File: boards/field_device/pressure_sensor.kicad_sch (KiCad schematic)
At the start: 4 parts, among them U3 SPA06-003

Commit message: fun
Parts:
- renumbered C6 to C8, C7 to C9, R6 to R9
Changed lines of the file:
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@@
 		(dnp no)
 		(fields_autoplaced yes)
-		(property "Reference" "#PWR012"
+		(property "Reference" "#PWR017"
 			(at 63.5 30.48 0)
 			(hide yes)
@@
 			(project "field_device"
 				(path "/99623870-118f-49fe-bbf0-fb0b890db442/ae167bff-0cee-4447-ad8b-23808a2f268b"
-					(reference "#PWR012")
+					(reference "#PWR017")
 					(unit 1)
 				)
@@
 		(dnp no)
 		(fields_autoplaced yes)
-		(property "Reference" "#PWR010"
+		(property "Reference" "#PWR015"
 			(at 30.48 26.67 0)
 			(hide yes)
@@
 			(project "field_device"
 				(path "/99623870-118f-49fe-bbf0-fb0b890db442/ae167bff-0cee-4447-ad8b-23808a2f268b"
-					(reference "#PWR010")
+					(reference "#PWR015")
 					(unit 1)
 				)
@@
 		(dnp no)
 		(fields_autoplaced yes)
-		(property "Reference" "C6"
+		(property "Reference" "C8"
 			(at 34.29 25.3999 0)
 			(show_name no)
@@
 			(project "field_device"
 				(path "/99623870-118f-49fe-bbf0-fb0b890db442/ae167bff-0cee-4447-ad8b-23808a2f268b"
-					(reference "C6")
+					(reference "C8")
 					(unit 1)
 				)
@@
 		(dnp no)
 		(fields_autoplaced yes)
-		(property "Reference" "#PWR013"
+		(property "Reference" "#PWR018"
 			(at 81.28 24.13 0)
 			(hide yes)
@@
 			(project "field_device"
 				(path "/99623870-118f-49fe-bbf0-fb0b890db442/ae167bff-0cee-4447-ad8b-23808a2f268b"
-					(reference "#PWR013")
+					(reference "#PWR018")
 					(unit 1)
 				)
@@
 		(dnp no)
 		(fields_autoplaced yes)
-		(property "Reference" "#PWR014"
+		(property "Reference" "#PWR019"
 			(at 116.84 26.67 0)
 			(hide yes)
@@
 			(project "field_device"
 				(path "/99623870-118f-49fe-bbf0-fb0b890db442/ae167bff-0cee-4447-ad8b-23808a2f268b"
-					(reference "#PWR014")
+					(reference "#PWR019")
 					(unit 1)
 				)
@@
 		(dnp no)
 		(fields_autoplaced yes)
-		(property "Reference" "R6"
+		(property "Reference" "R9"
 			(at 71.12 20.32 90)
 			(show_name no)
@@
 			(project "field_device"
 				(path "/99623870-118f-49fe-bbf0-fb0b890db442/ae167bff-0cee-4447-ad8b-23808a2f268b"
-					(reference "R6")
+					(reference "R9")
 					(unit 1)
 				)
@@
 		(dnp no)
 		(fields_autoplaced yes)
-		(property "Reference" "C7"
+		(property "Reference" "C9"
 			(at 46.99 25.3999 0)
 			(show_name no)
@@
 			(project "field_device"
 				(path "/99623870-118f-49fe-bbf0-fb0b890db442/ae167bff-0cee-4447-ad8b-23808a2f268b"
-					(reference "C7")
+					(reference "C9")
 					(unit 1)
 				)
@@
 		(dnp no)
 		(fields_autoplaced yes)
-		(property "Reference" "#PWR011"
+		(property "Reference" "#PWR016"
 			(at 30.48 36.83 0)
 			(hide yes)
@@
 			(project "field_device"
 				(path "/99623870-118f-49fe-bbf0-fb0b890db442/ae167bff-0cee-4447-ad8b-23808a2f268b"
-					(reference "#PWR011")
-					(unit 1)
-				)
+					(reference "#PWR016")
+					(unit 1)
+				)

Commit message: reorganized mcu
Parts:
- C8, C9: value 100nF -> 100n
- R9: value 10kΩ? -> 10k?
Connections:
- no-connect marks 0 -> 1
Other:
- moved on the sheet: C8, C9
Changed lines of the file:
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@@
 	(paper "A4")
 	(junction
-		(at 30.48 22.86)
+		(at 125.73 24.13)
 		(diameter 0)
 		(color 0 0 0 0)
 	)
 	(junction
-		(at 43.18 22.86)
+		(at 120.65 24.13)
 		(diameter 0)
 		(color 0 0 0 0)
 	)
 	(junction
-		(at 30.48 30.48)
+		(at 138.43 24.13)
 		(diameter 0)
 		(color 0 0 0 0)
 	)
+	(junction
+		(at 138.43 31.75)
+		(diameter 0)
+		(color 0 0 0 0)
+	)
+	(no_connect
+		(at 110.49 31.75)
+	)
 	(wire
 		(pts
@@
 	(wire
 		(pts
-			(xy 30.48 22.86) (xy 43.18 22.86)
+			(xy 125.73 24.13) (xy 138.43 24.13)
+		)
+		(stroke
+			(width 0)
+			(type default)
+		)
+	)
+	(wire
+		(pts
+			(xy 120.65 24.13) (xy 120.65 29.21)
 		)
 		(stroke
@@
 	(wire
 		(pts
-			(xy 43.18 22.86) (xy 45.72 22.86)
-		)
-		(stroke
-			(width 0)
-			(type default)
-		)
-	)
-	(wire
-		(pts
-			(xy 30.48 30.48) (xy 43.18 30.48)
-		)
-		(stroke
-			(width 0)
-			(type default)
-		)
-	)
-	(label "clean_pwr"
-		(at 110.49 24.13 0)
-		(effects
-			(font
-				(size 1.27 1.27)
-			)
-			(justify left bottom)
-		)
-	)
-	(label "clean_pwr"
-		(at 45.72 22.86 0)
-		(effects
-			(font
-				(size 1.27 1.27)
-			)
-			(justify left bottom)
-		)
-	)
-	(label "clean_pwr"
-		(at 110.49 29.21 0)
-		(effects
-			(font
-				(size 1.27 1.27)
-			)
-			(justify left bottom)
+			(xy 110.49 24.13) (xy 120.65 24.13)
+		)
+		(stroke
+			(width 0)
+			(type default)
+		)
+	)
+	(wire
+		(pts
+			(xy 125.73 31.75) (xy 138.43 31.75)
+		)
+		(stroke
+			(width 0)
+			(type default)
+		)
+	)
+	(wire
+		(pts
+			(xy 120.65 24.13) (xy 125.73 24.13)
+		)
+		(stroke
+			(width 0)
+			(type default)
+		)
+	)
+	(wire
+		(pts
+			(xy 120.65 29.21) (xy 110.49 29.21)
+		)
+		(stroke
+			(width 0)
+			(type default)
 		)
 	)
@@
 	(symbol
 		(lib_id "power:+3.3V")
-		(at 30.48 22.86 0)
+		(at 138.43 24.13 0)
 		(unit 1)
 		(body_style 1)
@@
 		(fields_autoplaced yes)
 		(property "Reference" "#PWR015"
-			(at 30.48 26.67 0)
+			(at 138.43 27.94 0)
 			(hide yes)
 			(show_name no)
@@
 		)
 		(property "Value" "+3.3V"
-			(at 30.48 17.78 0)
+			(at 138.43 19.05 0)
 			(show_name no)
 			(do_not_autoplace no)
@@
 		)
 		(property "Footprint" ""
-			(at 30.48 22.86 0)
+			(at 138.43 24.13 0)
 			(hide yes)
 			(show_name no)
@@
 		)
 		(property "Datasheet" ""
-			(at 30.48 22.86 0)
+			(at 138.43 24.13 0)
 			(hide yes)
 			(show_name no)
@@
 		)
 		(property "Description" "Power symbol creates a global label with name \"+3.3V\""
-			(at 30.48 22.86 0)
+			(at 138.43 24.13 0)
 			(hide yes)
 			(show_name no)
@@
 	(symbol
 		(lib_id "Device:C")
-		(at 30.48 26.67 0)
+		(at 125.73 27.94 0)
 		(unit 1)
 		(body_style 1)
@@
 		(fields_autoplaced yes)
 		(property "Reference" "C8"
-			(at 34.29 25.3999 0)
+			(at 129.54 26.6699 0)
 			(show_name no)
 			(do_not_autoplace no)
@@
 			)
 		)
-		(property "Value" "100nF"
-			(at 34.29 27.9399 0)
+		(property "Value" "100n"
+			(at 129.54 29.2099 0)
 			(show_name no)
 			(do_not_autoplace no)
@@
 		)
 		(property "Footprint" "Capacitor_SMD:C_0603_1608Metric"
-			(at 31.4452 30.48 0)
+			(at 126.6952 31.75 0)
 			(hide yes)
 			(show_name no)
@@
 		)
 		(property "Datasheet" ""
-			(at 30.48 26.67 0)
+			(at 125.73 27.94 0)
 			(hide yes)
 			(show_name no)
@@
 		)
 		(property "Description" "Unpolarized capacitor"
-			(at 30.48 26.67 0)
+			(at 125.73 27.94 0)
 			(hide yes)
 			(show_name no)
@@
 		)
 		(property "Field5" ""
-			(at 30.48 26.67 0)
+			(at 125.73 27.94 0)
 			(hide yes)
 			(show_name no)
@@
 		)
 		(property "Field6" ""
-			(at 30.48 26.67 0)
+			(at 125.73 27.94 0)
 			(hide yes)
 			(show_name no)
@@
 			)
 		)
-		(property "Value" "10kΩ?"
+		(property "Value" "10k?"
 			(at 71.12 22.86 90)
 			(show_name no)
@@
 	(symbol
 		(lib_id "Device:C")
-		(at 43.18 26.67 0)
+		(at 138.43 27.94 0)
 		(unit 1)
 		(body_style 1)
@@
 		(fields_autoplaced yes)
 		(property "Reference" "C9"
-			(at 46.99 25.3999 0)
+			(at 142.24 26.6699 0)
 			(show_name no)
 			(do_not_autoplace no)
@@
 			)
 		)
-		(property "Value" "100nF"
-			(at 46.99 27.9399 0)
+		(property "Value" "100n"
+			(at 142.24 29.2099 0)
 			(show_name no)
 			(do_not_autoplace no)
@@
 		)
 		(property "Footprint" "Capacitor_SMD:C_0603_1608Metric"
-			(at 44.1452 30.48 0)
+			(at 139.3952 31.75 0)
 			(hide yes)
 			(show_name no)
@@
 		)
 		(property "Datasheet" ""
-			(at 43.18 26.67 0)
+			(at 138.43 27.94 0)
 			(hide yes)
 			(show_name no)
@@
 		)
 		(property "Description" "Unpolarized capacitor"
-			(at 43.18 26.67 0)
+			(at 138.43 27.94 0)
 			(hide yes)
 			(show_name no)
@@
 	(symbol
 		(lib_id "power:GND")
-		(at 30.48 30.48 0)
+		(at 138.43 31.75 0)
 		(unit 1)
 		(body_style 1)
@@
 		(fields_autoplaced yes)
 		(property "Reference" "#PWR016"
-			(at 30.48 36.83 0)
+			(at 138.43 38.1 0)
 			(hide yes)
 			(show_name no)
@@
 		)
 		(property "Value" "GND"
-			(at 30.48 35.56 0)
+			(at 138.43 36.83 0)
 			(show_name no)
 			(do_not_autoplace no)
@@
 		)
 		(property "Footprint" ""
-			(at 30.48 30.48 0)
+			(at 138.43 31.75 0)
 			(hide yes)
 			(show_name no)
@@
 		)
 		(property "Datasheet" ""
-			(at 30.48 30.48 0)
+			(at 138.43 31.75 0)
 			(hide yes)
 			(show_name no)
@@
 		)
 		(property "Description" "Power symbol creates a global label with name \"GND\" , ground"
-			(at 30.48 30.48 0)
-			(hide yes)
-			(show_name no)
+			(at 138.43 31.75 0)
+			(hide yes)
+			(show_name no)

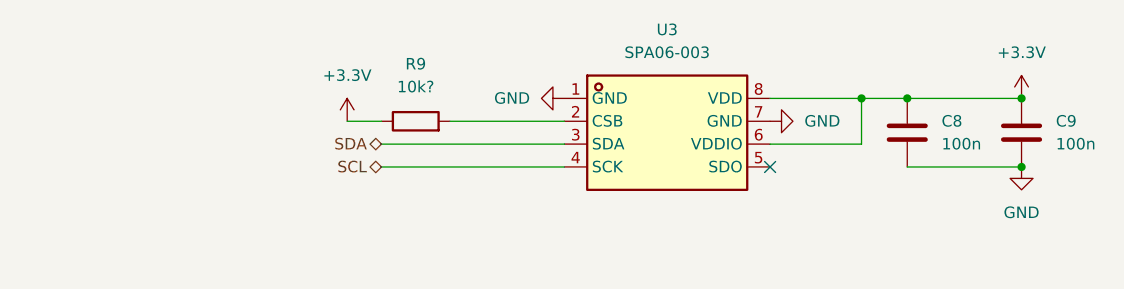
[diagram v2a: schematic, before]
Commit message: added satus leds
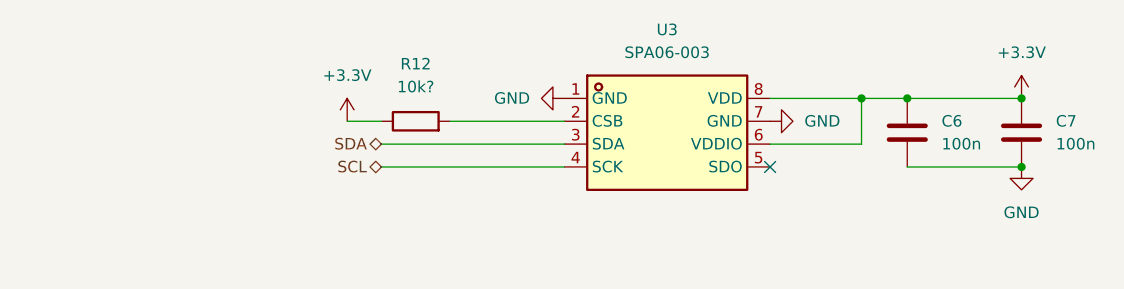
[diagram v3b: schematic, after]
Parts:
- renumbered C8 to C6, C9 to C7, R9 to R12
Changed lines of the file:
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@@
 		(dnp no)
 		(fields_autoplaced yes)
-		(property "Reference" "#PWR017"
+		(property "Reference" "#PWR014"
 			(at 63.5 30.48 0)
 			(hide yes)
@@
 			(project "field_device"
 				(path "/99623870-118f-49fe-bbf0-fb0b890db442/ae167bff-0cee-4447-ad8b-23808a2f268b"
-					(reference "#PWR017")
+					(reference "#PWR014")
 					(unit 1)
 				)
@@
 		(dnp no)
 		(fields_autoplaced yes)
-		(property "Reference" "#PWR015"
+		(property "Reference" "#PWR017"
 			(at 138.43 27.94 0)
 			(hide yes)
@@
 			(project "field_device"
 				(path "/99623870-118f-49fe-bbf0-fb0b890db442/ae167bff-0cee-4447-ad8b-23808a2f268b"
-					(reference "#PWR015")
+					(reference "#PWR017")
 					(unit 1)
 				)
@@
 		(dnp no)
 		(fields_autoplaced yes)
-		(property "Reference" "C8"
+		(property "Reference" "C6"
 			(at 129.54 26.6699 0)
 			(show_name no)
@@
 			(project "field_device"
 				(path "/99623870-118f-49fe-bbf0-fb0b890db442/ae167bff-0cee-4447-ad8b-23808a2f268b"
-					(reference "C8")
+					(reference "C6")
 					(unit 1)
 				)
@@
 		(dnp no)
 		(fields_autoplaced yes)
-		(property "Reference" "#PWR018"
+		(property "Reference" "#PWR015"
 			(at 81.28 24.13 0)
 			(hide yes)
@@
 			(project "field_device"
 				(path "/99623870-118f-49fe-bbf0-fb0b890db442/ae167bff-0cee-4447-ad8b-23808a2f268b"
-					(reference "#PWR018")
+					(reference "#PWR015")
 					(unit 1)
 				)
@@
 		(dnp no)
 		(fields_autoplaced yes)
-		(property "Reference" "#PWR019"
+		(property "Reference" "#PWR016"
 			(at 116.84 26.67 0)
 			(hide yes)
@@
 			(project "field_device"
 				(path "/99623870-118f-49fe-bbf0-fb0b890db442/ae167bff-0cee-4447-ad8b-23808a2f268b"
-					(reference "#PWR019")
+					(reference "#PWR016")
 					(unit 1)
 				)
@@
 		(dnp no)
 		(fields_autoplaced yes)
-		(property "Reference" "R9"
+		(property "Reference" "R12"
 			(at 71.12 20.32 90)
 			(show_name no)
@@
 			(project "field_device"
 				(path "/99623870-118f-49fe-bbf0-fb0b890db442/ae167bff-0cee-4447-ad8b-23808a2f268b"
-					(reference "R9")
+					(reference "R12")
 					(unit 1)
 				)
@@
 		(dnp no)
 		(fields_autoplaced yes)
-		(property "Reference" "C9"
+		(property "Reference" "C7"
 			(at 142.24 26.6699 0)
 			(show_name no)
@@
 			(project "field_device"
 				(path "/99623870-118f-49fe-bbf0-fb0b890db442/ae167bff-0cee-4447-ad8b-23808a2f268b"
-					(reference "C9")
+					(reference "C7")
 					(unit 1)
 				)
@@
 		(dnp no)
 		(fields_autoplaced yes)
-		(property "Reference" "#PWR016"
+		(property "Reference" "#PWR018"
 			(at 138.43 38.1 0)
 			(hide yes)
@@
 			(project "field_device"
 				(path "/99623870-118f-49fe-bbf0-fb0b890db442/ae167bff-0cee-4447-ad8b-23808a2f268b"
-					(reference "#PWR016")
-					(unit 1)
-				)
+					(reference "#PWR018")
+					(unit 1)
+				)

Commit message: i guess made schematic more readable?
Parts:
- C6, C7: footprint Capacitor_SMD:C_0603_1608Metric -> Capacitor_SMD:C_0603_1608Metric_Pad1.08x0.95mm_HandSolder
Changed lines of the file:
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@@
 			)
 		)
-		(property "Footprint" "Capacitor_SMD:C_0603_1608Metric"
+		(property "Footprint" "Capacitor_SMD:C_0603_1608Metric_Pad1.08x0.95mm_HandSolder"
 			(at 126.6952 31.75 0)
 			(hide yes)
@@
 			)
 		)
-		(property "Footprint" "Capacitor_SMD:C_0603_1608Metric"
+		(property "Footprint" "Capacitor_SMD:C_0603_1608Metric_Pad1.08x0.95mm_HandSolder"
 			(at 139.3952 31.75 0)
 			(hide yes)

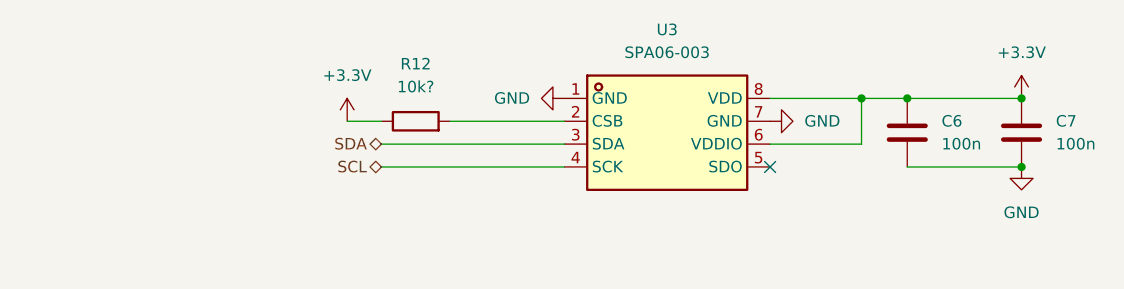
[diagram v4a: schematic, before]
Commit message: changed regulator
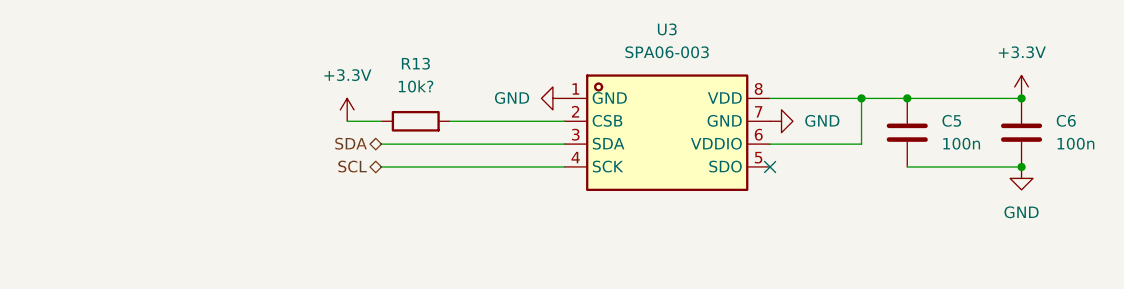
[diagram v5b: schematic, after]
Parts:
- C5: renamed from C6; footprint Capacitor_SMD:C_0603_1608Metric_Pad1.08x0.95mm_HandSolder -> Capacitor_SMD:C_0402_1005Metric_Pad0.74x0.62mm_HandSolder
- C6: renamed from C7; footprint Capacitor_SMD:C_0603_1608Metric_Pad1.08x0.95mm_HandSolder -> Capacitor_SMD:C_0402_1005Metric_Pad0.74x0.62mm_HandSolder
- R13: renamed from R12; footprint Resistor_SMD:R_0603_1608Metric -> Resistor_SMD:R_0402_1005Metric_Pad0.72x0.64mm_HandSolder
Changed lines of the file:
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@@
 		(dnp no)
 		(fields_autoplaced yes)
-		(property "Reference" "C6"
+		(property "Reference" "C5"
 			(at 129.54 26.6699 0)
 			(show_name no)
@@
 			)
 		)
-		(property "Footprint" "Capacitor_SMD:C_0603_1608Metric_Pad1.08x0.95mm_HandSolder"
+		(property "Footprint" "Capacitor_SMD:C_0402_1005Metric_Pad0.74x0.62mm_HandSolder"
 			(at 126.6952 31.75 0)
 			(hide yes)
@@
 			(project "field_device"
 				(path "/99623870-118f-49fe-bbf0-fb0b890db442/ae167bff-0cee-4447-ad8b-23808a2f268b"
-					(reference "C6")
+					(reference "C5")
 					(unit 1)
 				)
@@
 		(dnp no)
 		(fields_autoplaced yes)
-		(property "Reference" "R12"
+		(property "Reference" "R13"
 			(at 71.12 20.32 90)
 			(show_name no)
@@
 			)
 		)
-		(property "Footprint" "Resistor_SMD:R_0603_1608Metric"
+		(property "Footprint" "Resistor_SMD:R_0402_1005Metric_Pad0.72x0.64mm_HandSolder"
 			(at 71.12 28.448 90)
 			(hide yes)
@@
 			(project "field_device"
 				(path "/99623870-118f-49fe-bbf0-fb0b890db442/ae167bff-0cee-4447-ad8b-23808a2f268b"
-					(reference "R12")
+					(reference "R13")
 					(unit 1)
 				)
@@
 		(dnp no)
 		(fields_autoplaced yes)
-		(property "Reference" "C7"
+		(property "Reference" "C6"
 			(at 142.24 26.6699 0)
 			(show_name no)
@@
 			)
 		)
-		(property "Footprint" "Capacitor_SMD:C_0603_1608Metric_Pad1.08x0.95mm_HandSolder"
+		(property "Footprint" "Capacitor_SMD:C_0402_1005Metric_Pad0.74x0.62mm_HandSolder"
 			(at 139.3952 31.75 0)
 			(hide yes)
@@
 			(project "field_device"
 				(path "/99623870-118f-49fe-bbf0-fb0b890db442/ae167bff-0cee-4447-ad8b-23808a2f268b"
-					(reference "C7")
-					(unit 1)
-				)
+					(reference "C6")
+					(unit 1)
+				)

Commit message: route more stuff
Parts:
- C5, C6: footprint Capacitor_SMD:C_0402_1005Metric_Pad0.74x0.62mm_HandSolder -> Capacitor_SMD:C_0603_1608Metric
- R13: footprint Resistor_SMD:R_0402_1005Metric_Pad0.72x0.64mm_HandSolder -> Resistor_SMD:R_0603_1608Metric
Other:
- moved on the sheet: C5
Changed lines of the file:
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@@
 	(paper "A4")
 	(junction
-		(at 125.73 24.13)
-		(diameter 0)
-		(color 0 0 0 0)
-	)
-	(junction
-		(at 120.65 24.13)
+		(at 120.65 29.21)
 		(diameter 0)
 		(color 0 0 0 0)
@@
 		(color 0 0 0 0)
 	)
-	(junction
-		(at 138.43 31.75)
-		(diameter 0)
-		(color 0 0 0 0)
-	)
 	(no_connect
 		(at 110.49 31.75)
@@
 	(wire
 		(pts
-			(xy 125.73 24.13) (xy 138.43 24.13)
+			(xy 67.31 29.21) (xy 87.63 29.21)
 		)
 		(stroke
@@
 	(wire
 		(pts
-			(xy 120.65 24.13) (xy 120.65 29.21)
-		)
-		(stroke
-			(width 0)
-			(type default)
-		)
-	)
-	(wire
-		(pts
-			(xy 67.31 29.21) (xy 87.63 29.21)
-		)
-		(stroke
-			(width 0)
-			(type default)
-		)
-	)
-	(wire
-		(pts
-			(xy 110.49 24.13) (xy 120.65 24.13)
-		)
-		(stroke
-			(width 0)
-			(type default)
-		)
-	)
-	(wire
-		(pts
-			(xy 125.73 31.75) (xy 138.43 31.75)
-		)
-		(stroke
-			(width 0)
-			(type default)
-		)
-	)
-	(wire
-		(pts
-			(xy 120.65 24.13) (xy 125.73 24.13)
+			(xy 110.49 24.13) (xy 138.43 24.13)
 		)
 		(stroke
@@
 	(symbol
 		(lib_id "Device:C")
-		(at 125.73 27.94 0)
+		(at 120.65 33.02 0)
 		(unit 1)
 		(body_style 1)
@@
 		(fields_autoplaced yes)
 		(property "Reference" "C5"
-			(at 129.54 26.6699 0)
+			(at 124.46 31.7499 0)
 			(show_name no)
 			(do_not_autoplace no)
@@
 		)
 		(property "Value" "100n"
-			(at 129.54 29.2099 0)
+			(at 124.46 34.2899 0)
 			(show_name no)
 			(do_not_autoplace no)
@@
 			)
 		)
-		(property "Footprint" "Capacitor_SMD:C_0402_1005Metric_Pad0.74x0.62mm_HandSolder"
-			(at 126.6952 31.75 0)
-			(hide yes)
-			(show_name no)
-			(do_not_autoplace no)
-			(effects
-				(font
-					(size 1.27 1.27)
-				)
-			)
-		)
-		(property "Datasheet" ""
-			(at 125.73 27.94 0)
+		(property "Footprint" "Capacitor_SMD:C_0603_1608Metric"
+			(at 121.6152 36.83 0)
+			(hide yes)
+			(show_name no)
+			(do_not_autoplace no)
+			(effects
+				(font
+					(size 1.27 1.27)
+				)
+			)
+		)
+		(property "Datasheet" ""
+			(at 120.65 33.02 0)
 			(hide yes)
 			(show_name no)
@@
 		)
 		(property "Description" "Unpolarized capacitor"
-			(at 125.73 27.94 0)
+			(at 120.65 33.02 0)
 			(hide yes)
 			(show_name no)
@@
 		)
 		(property "Field5" ""
-			(at 125.73 27.94 0)
+			(at 120.65 33.02 0)
 			(hide yes)
 			(show_name no)
@@
 		)
 		(property "Field6" ""
-			(at 125.73 27.94 0)
+			(at 120.65 33.02 0)
 			(hide yes)
 			(show_name no)
@@
 			)
 		)
-		(property "Footprint" "Resistor_SMD:R_0402_1005Metric_Pad0.72x0.64mm_HandSolder"
+		(property "Footprint" "Resistor_SMD:R_0603_1608Metric"
 			(at 71.12 28.448 90)
 			(hide yes)
@@
 			)
 		)
-		(property "Footprint" "Capacitor_SMD:C_0402_1005Metric_Pad0.74x0.62mm_HandSolder"
+		(property "Footprint" "Capacitor_SMD:C_0603_1608Metric"
 			(at 139.3952 31.75 0)
 			(hide yes)
@@
 					(unit 1)
 				)
+			)
+		)
+	)
+	(symbol
+		(lib_id "power:GND")
+		(at 120.65 36.83 0)
+		(unit 1)
+		(body_style 1)
+		(exclude_from_sim no)
+		(in_bom yes)
+		(on_board yes)
+		(in_pos_files yes)
+		(dnp no)
+		(fields_autoplaced yes)
+		(property "Reference" "#PWR031"
+			(at 120.65 43.18 0)
+			(hide yes)
+			(show_name no)
+			(do_not_autoplace no)
+			(effects
+				(font
+					(size 1.27 1.27)
+				)
+			)
+		)
+		(property "Value" "GND"
+			(at 120.65 41.91 0)
+			(show_name no)
+			(do_not_autoplace no)
+			(effects
+				(font
+					(size 1.27 1.27)
+				)
+			)
+		)
+		(property "Footprint" ""
+			(at 120.65 36.83 0)
+			(hide yes)
+			(show_name no)
+			(do_not_autoplace no)
+			(effects
+				(font
+					(size 1.27 1.27)
+				)
+			)
+		)
+		(property "Datasheet" ""
+			(at 120.65 36.83 0)
+			(hide yes)
+			(show_name no)
+			(do_not_autoplace no)
+			(effects
+				(font
+					(size 1.27 1.27)
+				)
+			)
+		)
+		(property "Description" "Power symbol creates a global label with name \"GND\" , ground"
+			(at 120.65 36.83 0)
+			(hide yes)
+			(show_name no)
+			(do_not_autoplace no)
+			(effects
+				(font
+					(size 1.27 1.27)
+				)
+			)
+		)
+		(pin "1"
+		)
+		(instances
+			(project "field_device"
+				(path "/99623870-118f-49fe-bbf0-fb0b890db442/ae167bff-0cee-4447-ad8b-23808a2f268b"
+					(reference "#PWR031")
+					(unit 1)
+				)
+			)
+		)
+	)
+	(symbol
+		(lib_id "power:+3.3V")
+		(at 120.65 29.21 0)
+		(unit 1)
+		(body_style 1)
+		(exclude_from_sim no)
+		(in_bom yes)
+		(on_board yes)
+		(in_pos_files yes)
+		(dnp no)
+		(property "Reference" "#PWR032"
+			(at 120.65 33.02 0)
+			(hide yes)
+			(show_name no)
+			(do_not_autoplace no)
+			(effects
+				(font
+					(size 1.27 1.27)
+				)
+			)
+		)
+		(property "Value" "+3.3V"
+			(at 120.65 25.4 0)
+			(show_name no)
+			(do_not_autoplace no)
+			(effects
+				(font
+					(size 1.27 1.27)
+				)
+			)
+		)
+		(property "Footprint" ""
+			(at 120.65 29.21 0)
+			(hide yes)
+			(show_name no)
+			(do_not_autoplace no)
+			(effects
+				(font
+					(size 1.27 1.27)
+				)
+			)
+		)
+		(property "Datasheet" ""
+			(at 120.65 29.21 0)
+			(hide yes)
+			(show_name no)
+			(do_not_autoplace no)
+			(effects
+				(font
+					(size 1.27 1.27)
+				)
+			)
+		)
+		(property "Description" "Power symbol creates a global label with name \"+3.3V\""
+			(at 120.65 29.21 0)
+			(hide yes)
+			(show_name no)
+			(do_not_autoplace no)
+			(effects
+				(font
+					(size 1.27 1.27)
+				)
+			)
+		)
+		(pin "1"
+		)
+		(instances
+			(project "field_device"
+				(path "/99623870-118f-49fe-bbf0-fb0b890db442/ae167bff-0cee-4447-ad8b-23808a2f268b"
+					(reference "#PWR032")
+					(unit 1)
+				)
